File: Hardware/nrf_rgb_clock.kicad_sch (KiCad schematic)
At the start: 49 parts, among them J1 Conn_01x02, J3 Conn_01x07_Pin, U1 AMS1117-3.3, U3 TPS54260DGQ, Y1 32MHz

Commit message: finalized layout, via stitching
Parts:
- C17, C18: value ?p -> 18p; LCSC (none) -> C161409
- D116, D117: LCSC C965558 -> C114592
- L1: footprint LED_SMD:LED_0201_0603Metric -> LED_SMD:LED_0402_1005Metric; LCSC (none) -> C18221128
- L6: LCSC C42380964 -> C223066
- Y1: LCSC C37635386 -> C9009
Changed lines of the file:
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@@
 			)
 		)
-		(property "LCSC" "C965558"
+		(property "LCSC" "C114592"
 			(at 347.6341 50.8 0)
 			(effects
@@
 			)
 		)
-		(property "Value" "?p"
+		(property "Value" "18p"
 			(at 137.16 180.3462 0)
 			(effects
@@
 			)
 		)
+		(property "LCSC" "C161409"
+			(at 134.62 179.07 0)
+			(effects
+				(font
+					(size 1.27 1.27)
+				)
+				(hide yes)
+			)
+		)
 		(pin "1"
 		)
@@
 			)
 		)
-		(property "LCSC" "C965558"
+		(property "LCSC" "C114592"
 			(at 326.0441 50.8 0)
 			(effects
@@
 	)
 	(symbol
-		(lib_id "Device:C_Small")
-		(at 144.78 179.07 0)
-		(unit 1)
-		(exclude_from_sim no)
-		(in_bom yes)
-		(on_board yes)
-		(dnp no)
-		(fields_autoplaced yes)
-		(property "Reference" "C18"
-			(at 147.32 177.8062 0)
-			(effects
-				(font
-					(size 1.27 1.27)
-				)
-				(justify left)
-			)
-		)
-		(property "Value" "?p"
-			(at 147.32 180.3462 0)
-			(effects
-				(font
-					(size 1.27 1.27)
-				)
-				(justify left)
-			)
-		)
-		(property "Footprint" "Capacitor_SMD:C_0201_0603Metric"
-			(at 144.78 179.07 0)
-			(effects
-				(font
-					(size 1.27 1.27)
-				)
-				(hide yes)
-			)
-		)
-		(property "Datasheet" "~"
-			(at 144.78 179.07 0)
-			(effects
-				(font
-					(size 1.27 1.27)
-				)
-				(hide yes)
-			)
-		)
-		(property "Description" "Unpolarized capacitor, small symbol"
-			(at 144.78 179.07 0)
-			(effects
-				(font
-					(size 1.27 1.27)
-				)
-				(hide yes)
-			)
-		)
-		(property "MFN" ""
-			(at 144.78 179.07 0)
-			(effects
-				(font
-					(size 1.27 1.27)
-				)
-				(hide yes)
-			)
-		)
-		(pin "1"
-		)
-		(pin "2"
-		)
-		(instances
-			(project "nrf_rgb_clock"
-				(path "/80f7418f-7da9-43c7-b9f4-1e4eb07741f5"
-					(reference "C18")
-					(unit 1)
-				)
-			)
-		)
-	)
-	(symbol
 		(lib_id "power:GND")
 		(at 166.37 138.43 0)
@@
 			)
 		)
-		(property "LCSC" "C37635386"
+		(property "LCSC" "C9009"
 			(at 165.1 173.99 90)
 			(effects
@@
 			)
 		)
-		(property "LCSC" "C42380964"
+		(property "LCSC" "C223066 "
 			(at 99.06 62.23 90)
 			(effects
@@
 			)
 		)
-		(property "Footprint" "LED_SMD:LED_0201_0603Metric"
+		(property "Footprint" "LED_SMD:LED_0402_1005Metric"
 			(at 166.37 110.49 0)
 			(effects
@@
 			)
 		)
-		(property "LCSC" ""
+		(property "LCSC" "C18221128"
 			(at 166.37 110.49 0)
 			(effects
@@
 					(unit 1)
 				)
+			)
+		)
+	)
+	(symbol
+		(lib_id "Device:C_Small")
+		(at 144.78 179.07 0)
+		(unit 1)
+		(exclude_from_sim no)
+		(in_bom yes)
+		(on_board yes)
+		(dnp no)
+		(fields_autoplaced yes)
+		(property "Reference" "C18"
+			(at 147.32 177.8062 0)
+			(effects
+				(font
+					(size 1.27 1.27)
+				)
+				(justify left)
+			)
+		)
+		(property "Value" "18p"
+			(at 147.32 180.3462 0)
+			(effects
+				(font
+					(size 1.27 1.27)
+				)
+				(justify left)
+			)
+		)
+		(property "Footprint" "Capacitor_SMD:C_0201_0603Metric"
+			(at 144.78 179.07 0)
+			(effects
+				(font
+					(size 1.27 1.27)
+				)
+				(hide yes)
+			)
+		)
+		(property "Datasheet" "~"
+			(at 144.78 179.07 0)
+			(effects
+				(font
+					(size 1.27 1.27)
+				)
+				(hide yes)
+			)
+		)
+		(property "Description" "Unpolarized capacitor, small symbol"
+			(at 144.78 179.07 0)
+			(effects
+				(font
+					(size 1.27 1.27)
+				)
+				(hide yes)
+			)
+		)
+		(property "MFN" ""
+			(at 144.78 179.07 0)
+			(effects
+				(font
+					(size 1.27 1.27)
+				)
+				(hide yes)
+			)
+		)
+		(property "LCSC" "C161409"
+			(at 144.78 179.07 0)
+			(effects
+				(font
+					(size 1.27 1.27)
+				)
+				(hide yes)
+			)
+		)
+		(pin "1"
+		)
+		(pin "2"
+		)
+		(instances
+			(project "nrf_rgb_clock"
+				(path "/80f7418f-7da9-43c7-b9f4-1e4eb07741f5"
+					(reference "C18")
+					(unit 1)
+				)

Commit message: changed antenna
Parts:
- AE1: footprint ProjectFootprints:2450AT43A100E -> ProjectFootprints:2450AT18A100; LCSC C2917720 -> C89334
- D175: lcsc (none) -> C12632
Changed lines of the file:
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@@
 			)
 		)
-		(property "Footprint" "ProjectFootprints:2450AT43A100E"
+		(property "Footprint" "ProjectFootprints:2450AT18A100"
 			(at 238.76 167.005 0)
 			(effects
@@
 			)
 		)
-		(property "Datasheet" "https://www.lcsc.com/datasheet/lcsc_datasheet_2404021210_Johanson-Dielectrics-2450AT43A100E_C2917720.pdf"
+		(property "Datasheet" "https://www.lcsc.com/datasheet/lcsc_datasheet_2410122023_Johanson-Dielectrics-2450AT18A100E_C89334.pdf"
 			(at 238.76 167.005 0)
 			(effects
@@
 			)
 		)
-		(property "LCSC" "C2917720"
+		(property "LCSC" "C89334"
 			(at 241.3 171.45 0)
 			(effects
@@
 			(effects
 				(font
+					(size 1.27 1.27)
+				)
+				(hide yes)
+			)
+		)
+		(property "lcsc" "C12632"
+			(at 88.9 55.88 90)
+			(effects
+				(font

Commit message: removed d* reference designators
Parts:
- J1: lcsc (none) -> C8269
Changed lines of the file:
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@@
+			)
+		)
+		(property "lcsc" "C8269"
+			(at 26.67 123.19 0)
+			(effects
+				(font
+					(size 1.27 1.27)
+				)
+				(hide yes)
 			)
 		)

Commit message: finalized layout
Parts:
- J1: LCSC (none) -> C8269; lcsc C8269 -> (none)
- R12: LCSC C2930296 -> C105872
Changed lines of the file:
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@@
 			)
 		)
-		(property "lcsc" "C8269"
+		(property "LCSC" "C8269"
 			(at 26.67 123.19 0)
 			(effects
@@
 			)
 		)
-		(property "LCSC" "C2930296"
+		(property "LCSC" "C105872"
 			(at 129.54 77.47 0)
 			(effects

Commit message: updated lcsc numbers
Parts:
- AE1: lcsc_new (none) -> C127629
- C1: lcsc_new (none) -> C2932476
- C17, C18: lcsc_new (none) -> C161409
- C19, C2, C20, C3: lcsc_new (none) -> C696907
- C21: lcsc_new (none) -> C1525
- C22, C23: lcsc_new (none) -> C1710
- C24, C25: lcsc_new (none) -> C29823
- C26: lcsc_new (none) -> C15195
- C28: lcsc_new (none) -> C1588
- C4, C5: lcsc_new (none) -> C7432769
- C6: lcsc_new (none) -> C5142551
- C7: lcsc_new (none) -> C22374845
- C8, C9: lcsc_new (none) -> C22374839
- D116, D117: lcsc_new (none) -> C114592
- D175: LCSC (none) -> C12632; lcsc_new (none) -> C12632
- FB1: lcsc_new (none) -> C337874
- J1: lcsc_new (none) -> C8269
- L1: lcsc_new (none) -> C18221128
- L2: LCSC (none) -> C412057
- L3: LCSC (none) -> C108240
- L4: LCSC (none) -> C237447
- L6: lcsc_new (none) -> C223066
- R10: lcsc_new (none) -> C4328
- R11: lcsc_new (none) -> C2907247
- R12: lcsc_new (none) -> C105872
- R5: lcsc_new (none) -> C149504
- R7: lcsc_new (none) -> C25744
- R9: lcsc_new (none) -> C22375107
- U1: LCSC (none) -> C2891839; lcsc_new (none) -> C2891839
- U3: lcsc_new (none) -> C51800
- U4: lcsc_new (none) -> C42458750
- Y1: lcsc_new (none) -> C9009

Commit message: new tps
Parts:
- removed C21: 100n, Capacitor_SMD:C_0402_1005Metric, symbol Device:C_Small
- removed C22, C23: 47u 6.3V, Capacitor_SMD:C_0805_2012Metric, symbol Device:C_Small
- removed C24, C25: 4u7 100VDC, Capacitor_SMD:C_1206_3216Metric, symbol Device:C_Small
- removed C26: 10n, Capacitor_SMD:C_0402_1005Metric, symbol Device:C_Small
- removed C27: ~, Capacitor_SMD:C_0603_1608Metric, symbol Device:C_Small
- removed C28: 4n7, Capacitor_SMD:C_0603_1608Metric, symbol Device:C_Small
- removed D175: B360, Diode_SMD:D_SMC, symbol Diode:B360
- removed L6: 10u, ProjectFootprints:NRS5040T3R3NMGJV, symbol Device:L_Small
- removed R10: 20k, Resistor_SMD:R_0805_2012Metric, symbol Device:R_Small
- removed R11: 27k, Resistor_SMD:R_0805_2012Metric, symbol Device:R_Small
- removed R12: 5.1k, Resistor_SMD:R_0402_1005Metric, symbol Device:R_Small
- removed R5: 110k, Resistor_SMD:R_0805_2012Metric, symbol Device:R_Small
- removed R7: 10k, Resistor_SMD:R_0402_1005Metric, symbol Device:R_Small
- removed R9: 412k, Resistor_SMD:R_0805_2012Metric, symbol Device:R_Small
- removed U3: TPS54260DGQ, Package_SO:MSOP-10-1EP_3x3mm_P0.5mm_EP2.2x3.1mm_Mask1.83x1.89mm_ThermalVias, symbol Regulator_Switching:TPS54260DGQ
- added C10: 100n 50VDC, Capacitor_SMD:C_0805_2012Metric, symbol Device:C_Small
- added C11, C12, C13: 47u 6.3V, Capacitor_SMD:C_0805_2012Metric, symbol Device:C_Small
- added C14, C15: 4u7 100VDC, Capacitor_SMD:C_1206_3216Metric, symbol Device:C_Small
- added C16: 4n7 50VDC, Capacitor_SMD:C_0805_2012Metric, symbol Device:C_Small
- added C29: 47n 50VDC, Capacitor_SMD:C_0805_2012Metric, symbol Device:C_Small
- added D174: B560C, Diode_SMD:D_SMC, symbol Device:D_Schottky_Small_Filled
- added L7: 10u 7.8A, Inductor_SMD:L_Sunlord_MWSA1003S, symbol Device:L_Small
- added R1: 53k6, Resistor_SMD:R_0805_2012Metric, symbol Device:R_Small
- added R2: 10k2, Resistor_SMD:R_0805_2012Metric, symbol Device:R_Small
- added R3: 19k9, Resistor_SMD:R_0805_2012Metric, symbol Device:R_Small
- added R4: 243k, Resistor_SMD:R_0805_2012Metric, symbol Device:R_Small
- added U2: TPS54560BDDA, Package_SO:Texas_R-PDSO-G8_EP2.95x4.9mm_Mask2.4x3.1mm_ThermalVias, symbol Regulator_Switching:TPS54560BDDA
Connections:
- net +5V: now also C11.1, C12.1, C13.1, L7.2, R1.1
- net GND: now also C11.2, C12.2, C13.2, C14.2, C15.2, C16.2, C29.2, D174.2 (A), R2.2, R4.2, U2.7 (GND), U2.9 (GND)
- net V_EXT: now also C14.1, C15.1, U2.2 (VIN)
- new net: C10.2, D174.1 (K), L7.1, U2.8 (SW)
- new net: R4.1, U2.4 (RT/CLK)
- new net: C10.1, U2.1 (BOOT)
- new net: C16.1, R3.2
- new net: C29.1, R3.1, U2.6 (COMP)
- new net TPS_FB: R1.2, R2.1, U2.5 (FB)
- no-connect marks 3 -> 4

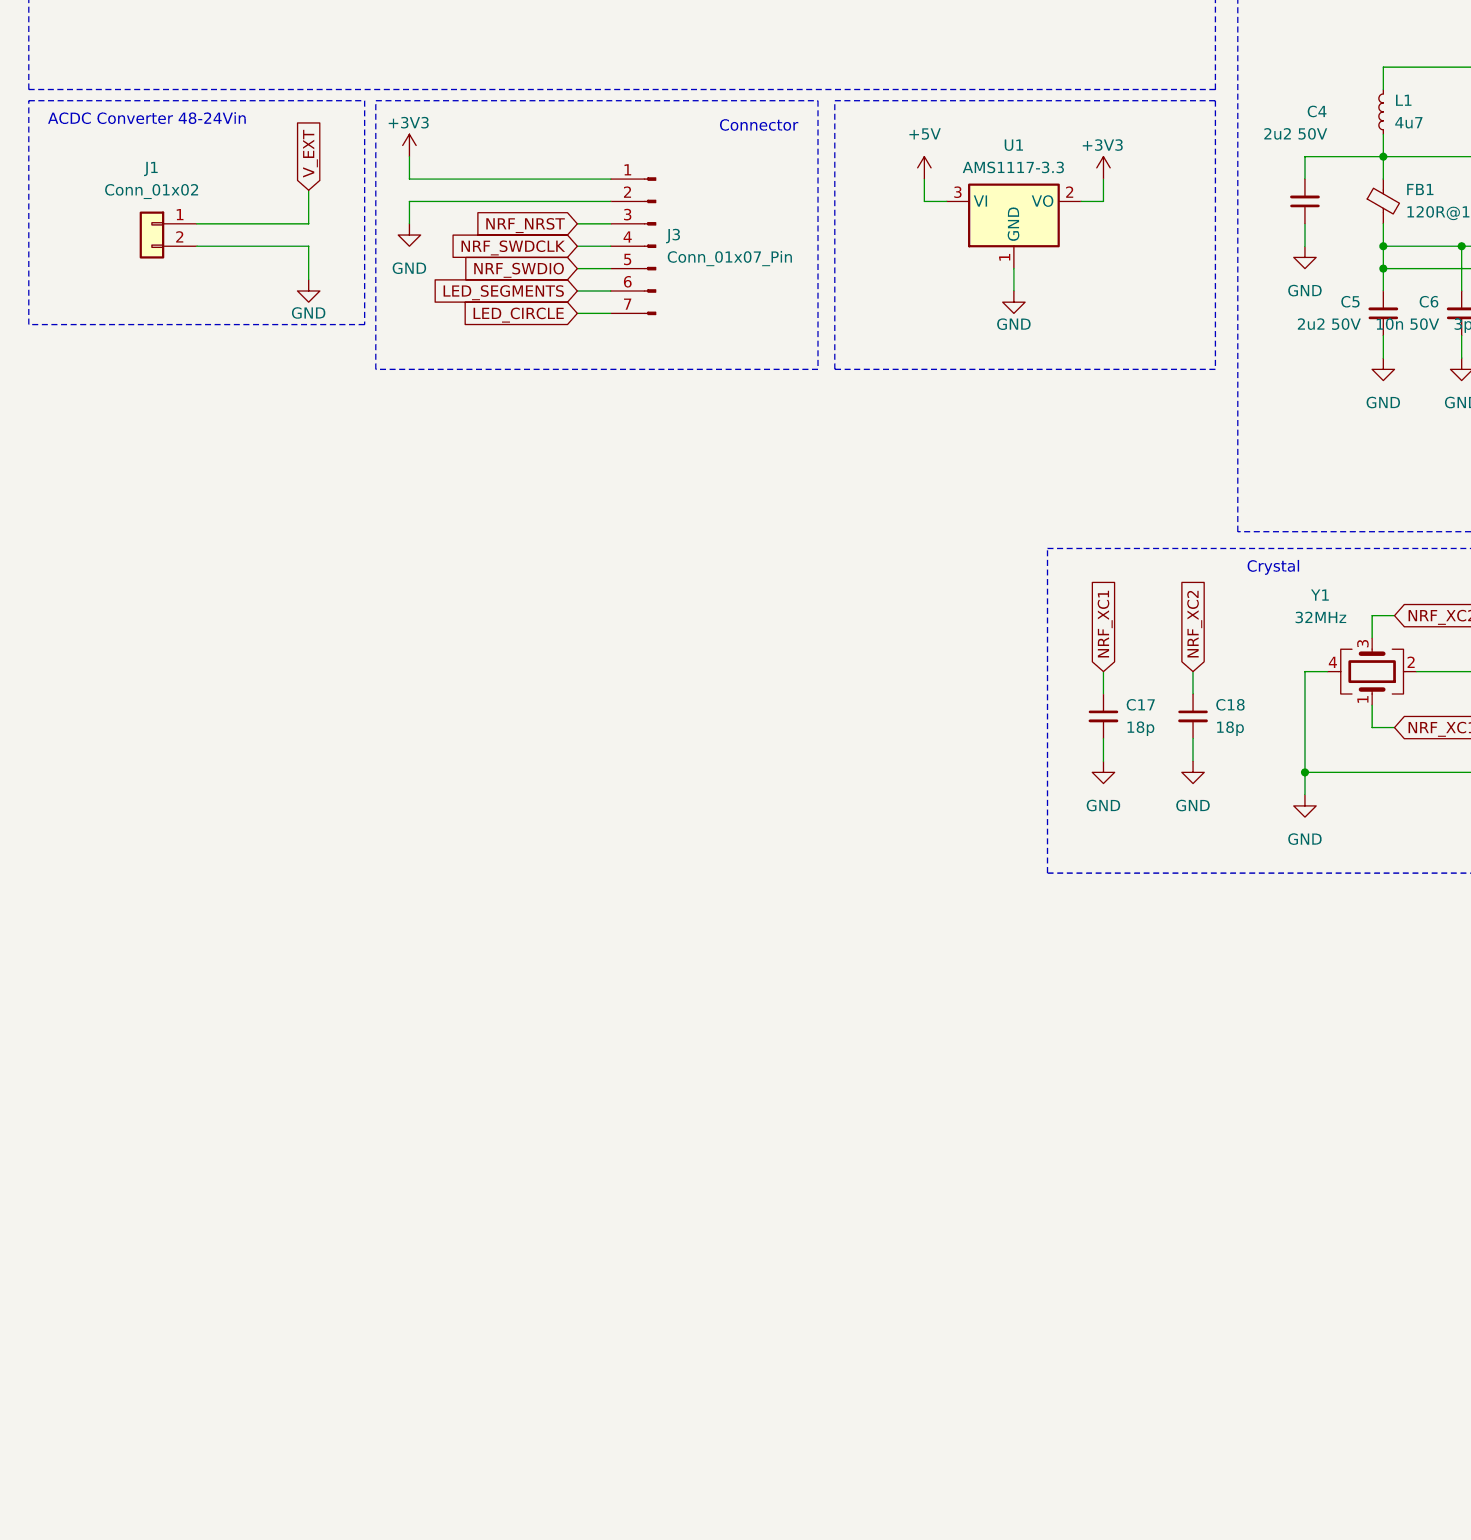
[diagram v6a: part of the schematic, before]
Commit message: added battery and rtc
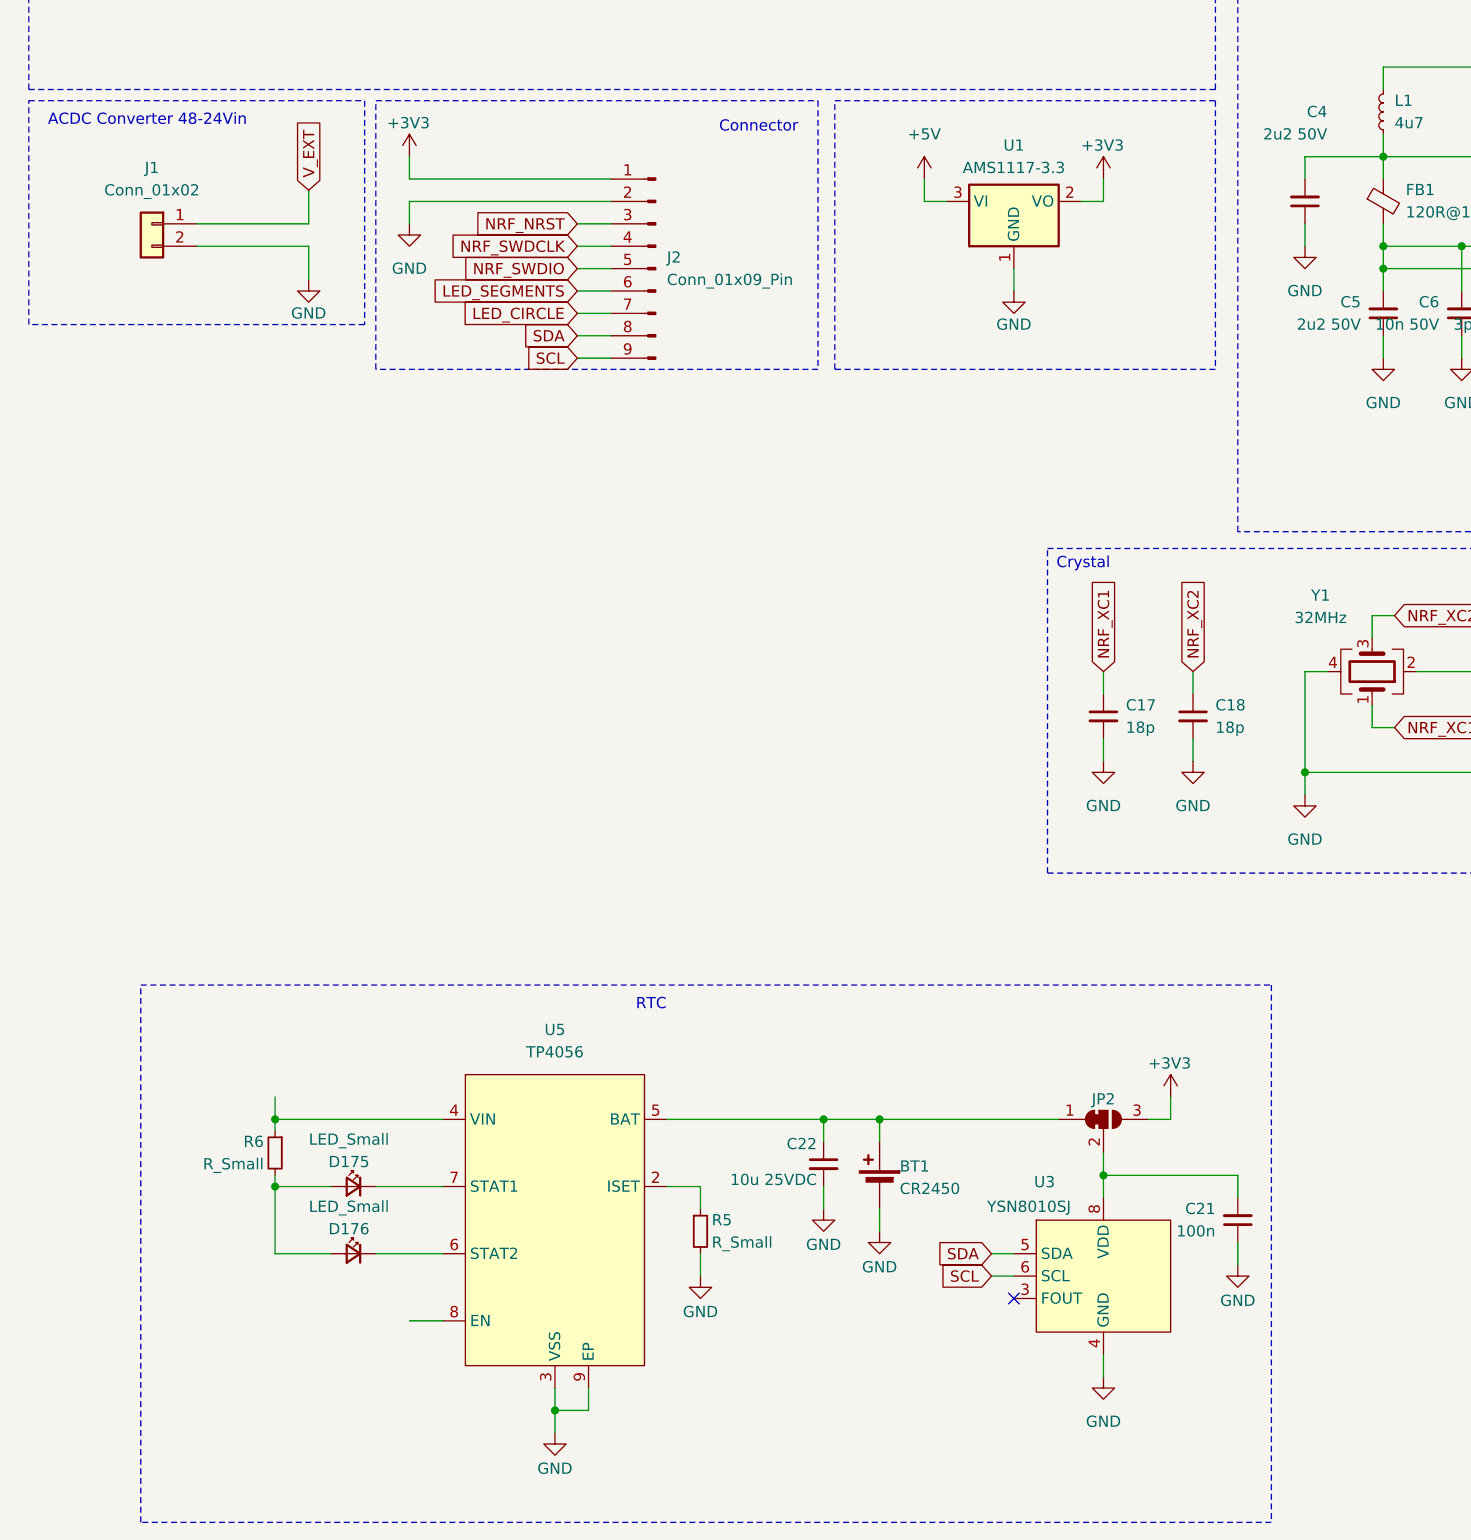
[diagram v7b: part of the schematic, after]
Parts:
- removed J3: Conn_01x07_Pin, Connector_PinHeader_2.54mm:PinHeader_1x07_P2.54mm_Vertical, symbol Connector:Conn_01x07_Pin
- added BT1: CR2450, Battery:BatteryHolder_ComfortableElectronic_CH273-2450_1x2450, symbol Device:Battery_Cell
- added C21: 100n, Capacitor_SMD:C_0402_1005Metric, symbol Device:C_Small
- added C22: 10u 25VDC, Capacitor_SMD:C_0805_2012Metric, symbol Device:C_Small
- added D175, D176: LED_Small, symbol Device:LED_Small
- added J2: Conn_01x09_Pin, Connector_PinHeader_2.54mm:PinHeader_1x09_P2.54mm_Vertical, symbol Connector:Conn_01x09_Pin
- added JP2: ~, Jumper:SolderJumper-3_P1.3mm_Bridged2Bar12_RoundedPad1.0x1.5mm_NumberLabels, symbol Jumper:SolderJumper_3_Bridged12
- added R5, R6: R_Small, symbol Device:R_Small
- added U3: YSN8010SJ, Package_SO:SOP-8_3.9x4.9mm_P1.27mm, symbol ProjectSymbols:YSN8010SJ
- added U5: TP4056, Package_SO:SOP-8_3.9x4.9mm_P1.27mm, symbol ProjectSymbols:tp4056
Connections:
- net +3V3: now also J2.1 (Pin_1), JP2.3 (B)
- net GND: now also BT1.2 (-), C21.1, C22.2, J2.2 (Pin_2), R5.2, U3.4 (GND), U5.3 (VSS), U5.9 (EP)
- net LED_CIRCLE: now also J2.7 (Pin_7)
- net LED_SEGMENTS: now also J2.6 (Pin_6)
- net NRF_NRST: now also J2.3 (Pin_3)
- net NRF_SWDCLK: now also J2.4 (Pin_4)
- net NRF_SWDIO: now also J2.5 (Pin_5)
- new net: D175.1 (K), U5.7 (STAT1)
- new net: D175.2 (A), D176.2 (A), R6.2
- new net: R6.1, U5.4 (VIN)
- new net: C21.2, JP2.2 (C), U3.8 (VDD)
- new net: BT1.1 (+), C22.1, JP2.1 (A), U5.5 (BAT)
- new net: D176.1 (K), U5.6 (STAT2)
- new net: U3.1 (T1), U3.2 (T2), U3.7 (T3)
- new net: R5.1, U5.2 (ISET)
- new net SCL: J2.9 (Pin_9), U3.6 (SCL)
- new net SDA: J2.8 (Pin_8), U3.5 (SDA)
- no-connect marks 4 -> 5
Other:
- note added: "RTC"
